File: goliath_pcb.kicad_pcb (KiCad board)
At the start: 2 copper layers, 140 x 90 mm, 95 parts, among them IC1 MCT9001, IC2 MCT9001SD, IC3 MCT9001SD, IC4 MCT9001SD, IC5 MCT9001SD, IC6 MCT9001SD, IC7 MCT9001SD, J1 RJ45_LED, J10 Conn_01x04_Male, J11 Screw_Terminal_01x02, J12 Screw_Terminal_01x02, J13 Screw_Terminal_01x02, J14 Conn_01x02_Male, J15 Conn_01x02_Male, J2 RJ45_LED, J3 RJ45_LED, J4 RJ45_LED, J5 Conn_01x08_Male, J6 Conn_01x08_Male, J7 Conn_01x02_Male, J8 Conn_01x04_Male, J9 Conn_01x04_Male, Q1 STP2N80K5, Q2 STP2N80K5, U1 Pico, U2 LM2592HVT-5.0/NOPB, U3 74HCT244, U4 74HCT244, U5 MCP3008, U6 PCF8574, U7 PCF8574

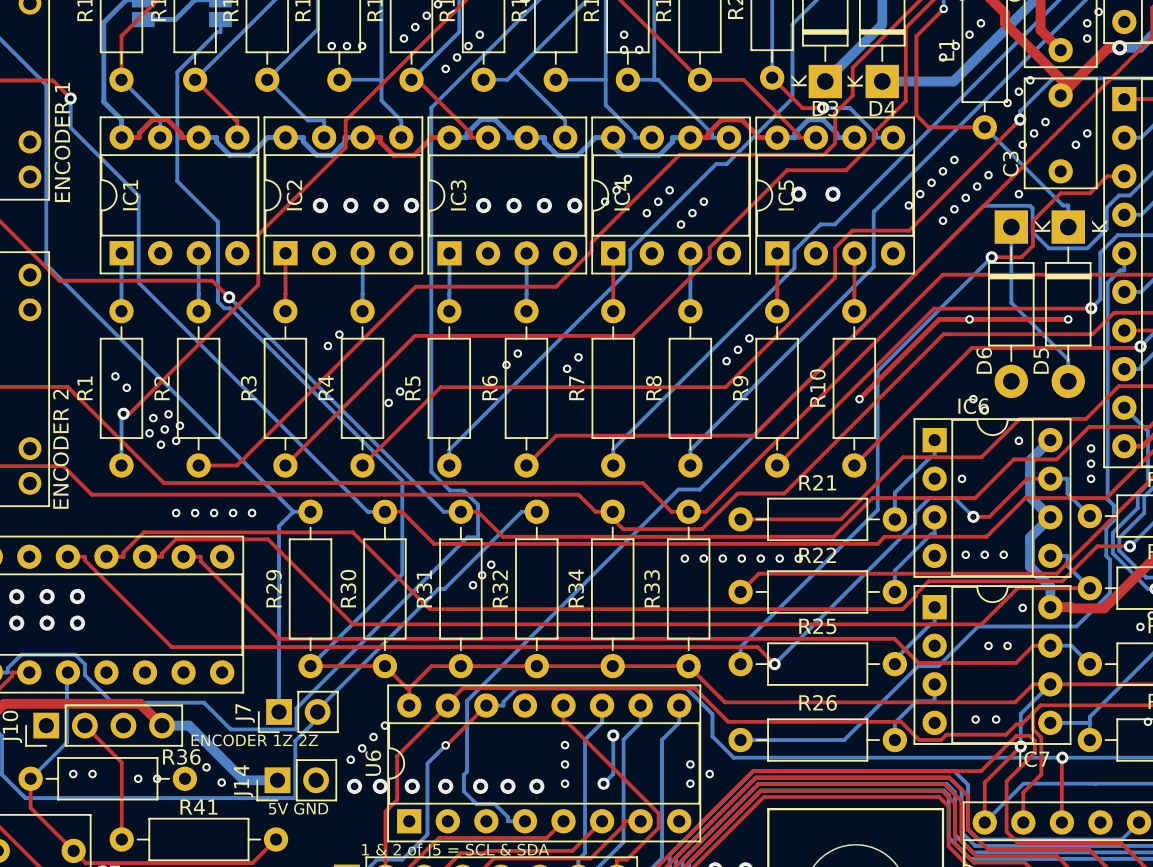
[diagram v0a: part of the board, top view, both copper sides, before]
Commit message: Clean up schematic
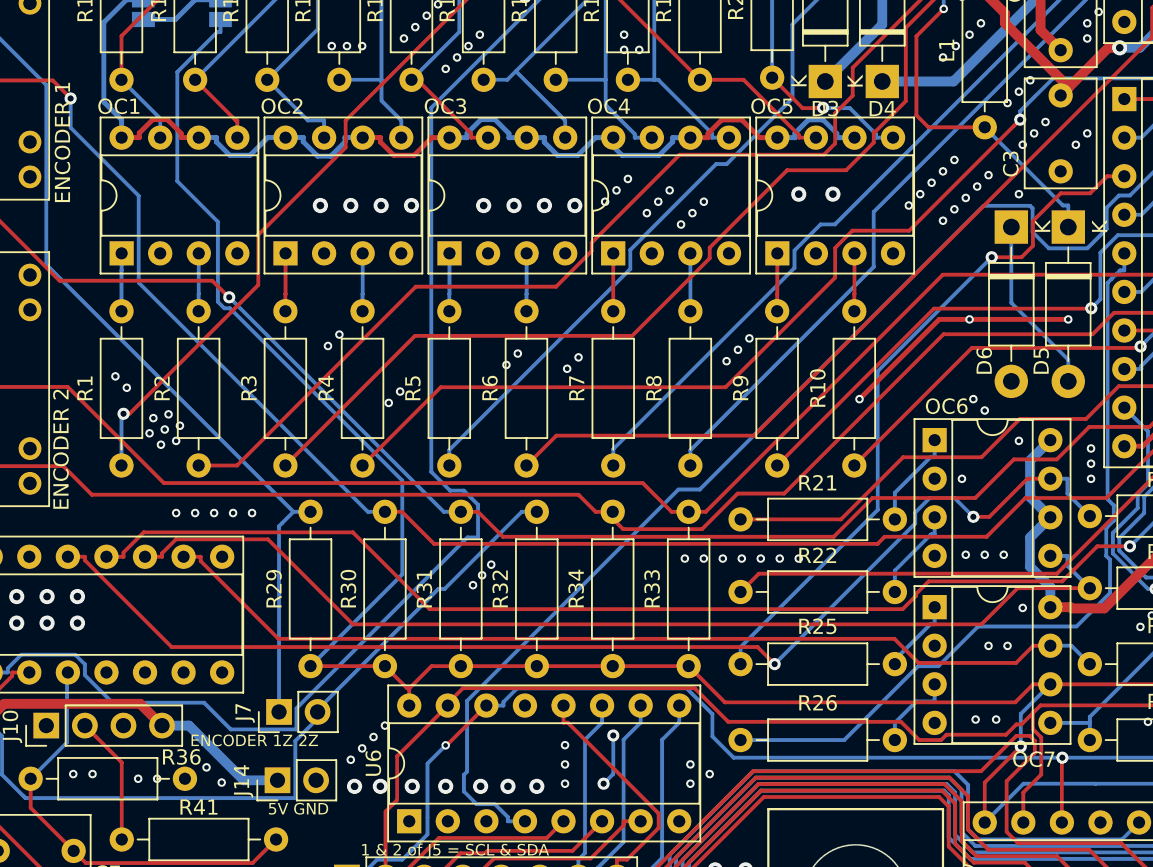
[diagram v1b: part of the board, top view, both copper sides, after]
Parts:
- OC2: renamed from IC2; value MCT9001SD -> MCT9001
- OC3: renamed from IC3; value MCT9001SD -> MCT9001
- OC4: renamed from IC4; value MCT9001SD -> MCT9001
- OC5: renamed from IC5; value MCT9001SD -> MCT9001
- OC6: renamed from IC6; value MCT9001SD -> MCT9001
- OC7: renamed from IC7; value MCT9001SD -> MCT9001
- renumbered IC1 to OC1

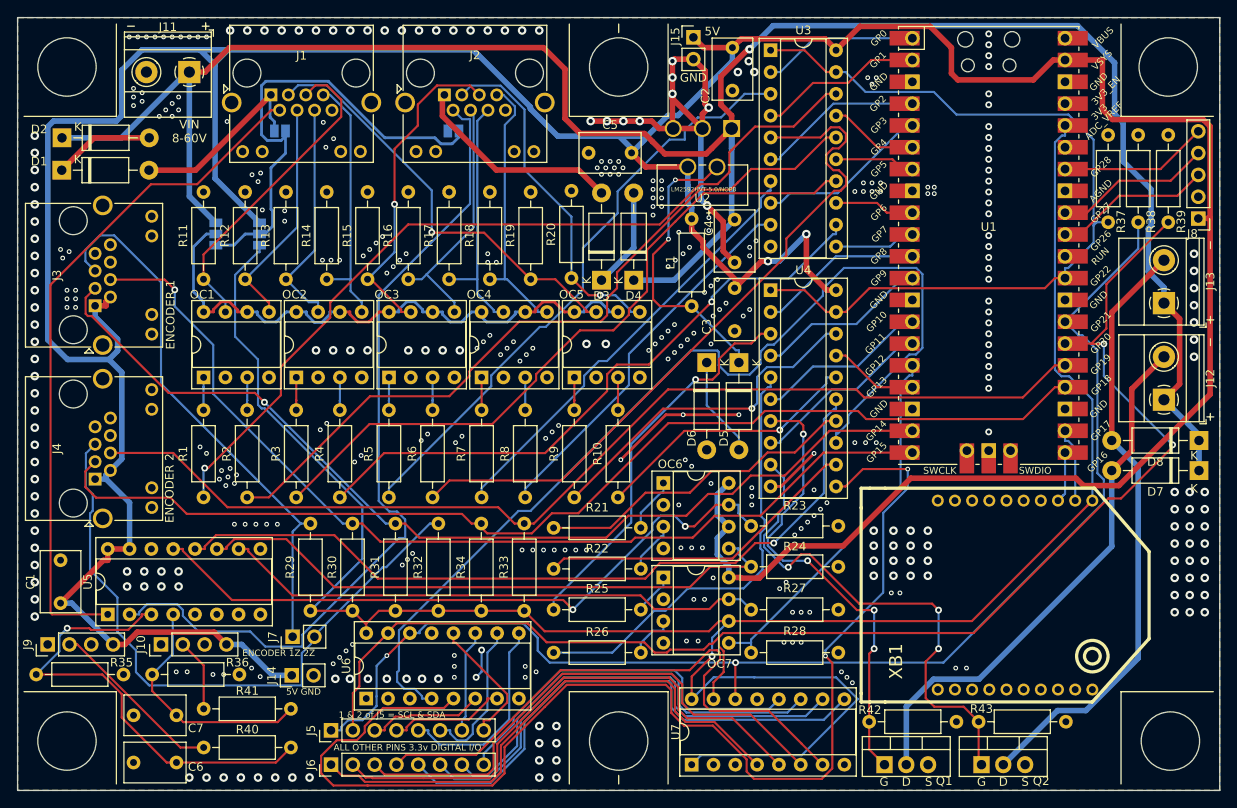
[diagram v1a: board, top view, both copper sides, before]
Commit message: Add proper M4 mounting holes
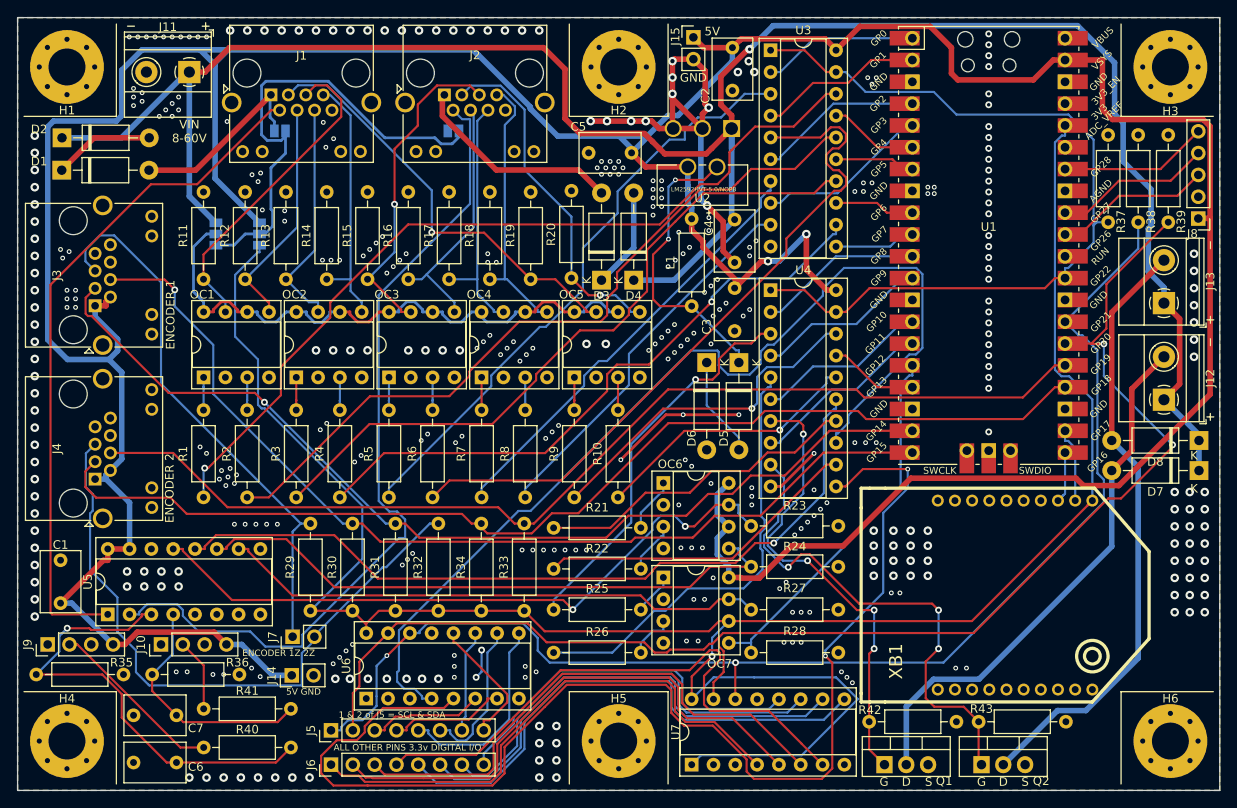
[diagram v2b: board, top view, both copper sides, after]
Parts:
- added H1: MountingHole_Pad, MountingHole:MountingHole_4.3mm_M4_Pad_Via, F.Cu at (41.2, 52.8)
- added H2: MountingHole_Pad, MountingHole:MountingHole_4.3mm_M4_Pad_Via, F.Cu at (105.5, 52.8)
- added H3: MountingHole_Pad, MountingHole:MountingHole_4.3mm_M4_Pad_Via, F.Cu at (169.8, 52.8)
- added H4: MountingHole_Pad, MountingHole:MountingHole_4.3mm_M4_Pad_Via, F.Cu at (41.2, 131.2)
- added H5: MountingHole_Pad, MountingHole:MountingHole_4.3mm_M4_Pad_Via, F.Cu at (105.5, 131.2)
- added H6: MountingHole_Pad, MountingHole:MountingHole_4.3mm_M4_Pad_Via, F.Cu at (169.8, 131.2)
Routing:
- net GND: vias 400 -> 397
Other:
- outline, holes or cut-outs redrawn

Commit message: Fix silkscreen issues
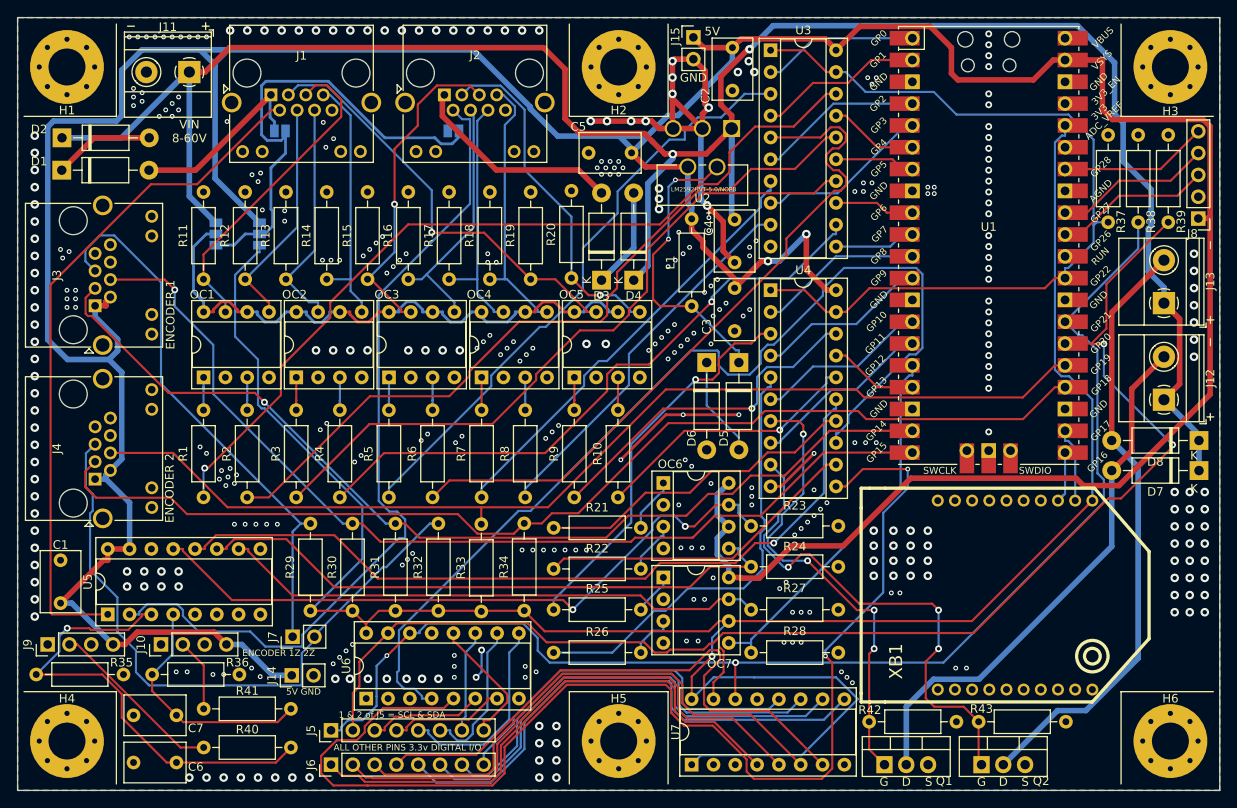
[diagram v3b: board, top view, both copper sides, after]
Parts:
- moved R33 5.00 mm to (89.5, 116.2)
- moved R34 5.00 mm to (94.5, 116.1)
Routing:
- net VIN: track 249.4 -> 251.3 mm, vias 1 -> 2
- net Net-(J4-Pad4): track 123.0 -> 123.9 mm
- net GND: vias 397 -> 391
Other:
- board text added: "Designed by Amelia Deck for ILLINOIS TECH ROBOTICS Robot Interfacing Board (RIB) V1.0-RC1"
- board text removed: "Designed by Amelia Deck for ILLINOIS TECH ROBOTICS Robot interfacing PCB V1.0-RC1"

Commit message: Prepare to swap out diodes
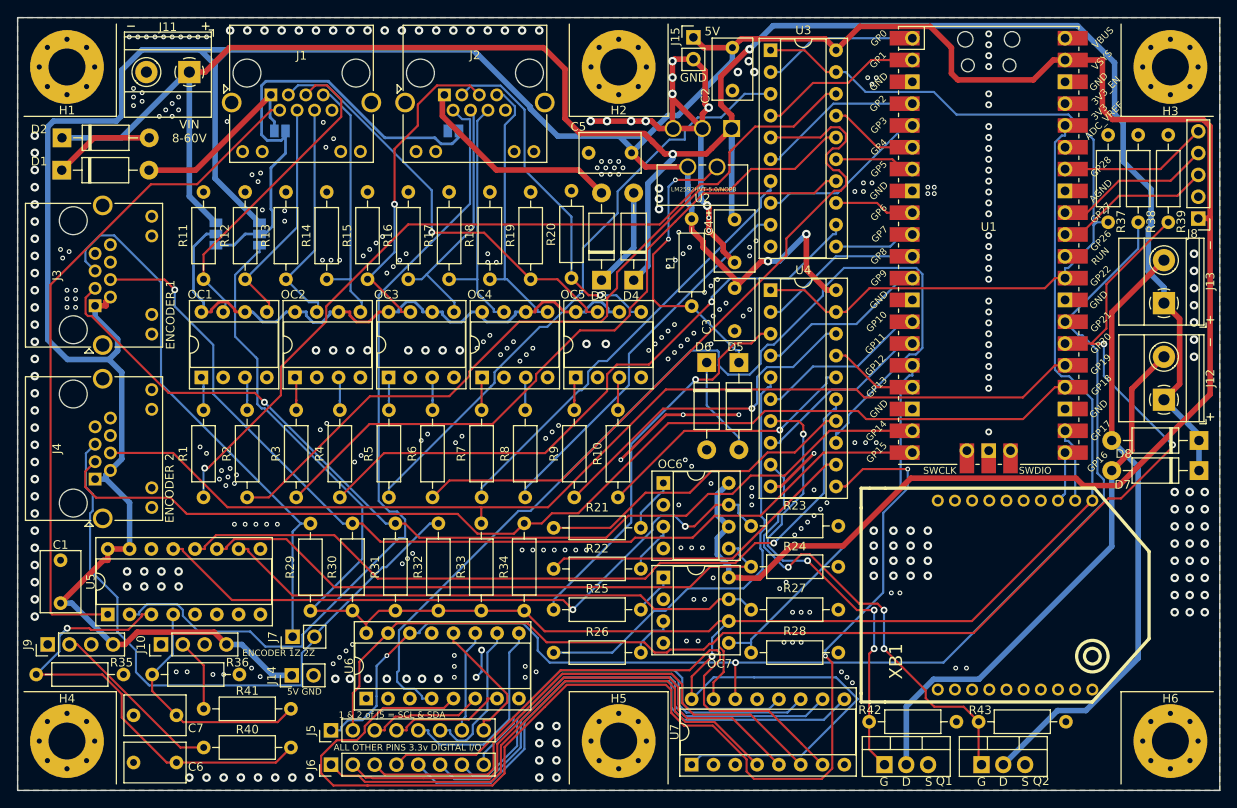
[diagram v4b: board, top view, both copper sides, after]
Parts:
- moved OC1 0.26 mm to (56.9, 88.9)
- moved OC5 0.16 mm to (100.5, 88.9)
- moved OC2 0.16 mm to (67.8, 88.9)
- moved R33 0.10 mm to (89.5, 116.1)
- moved OC4 0.06 mm to (89.6, 88.9)
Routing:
- net Net-(Q2-Pad1): track 59.1 -> 54.2 mm
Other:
- board text added: "GP28 GP27 GP26 GND 5V"

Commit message: Switch to better diodes, use via stitching plugin
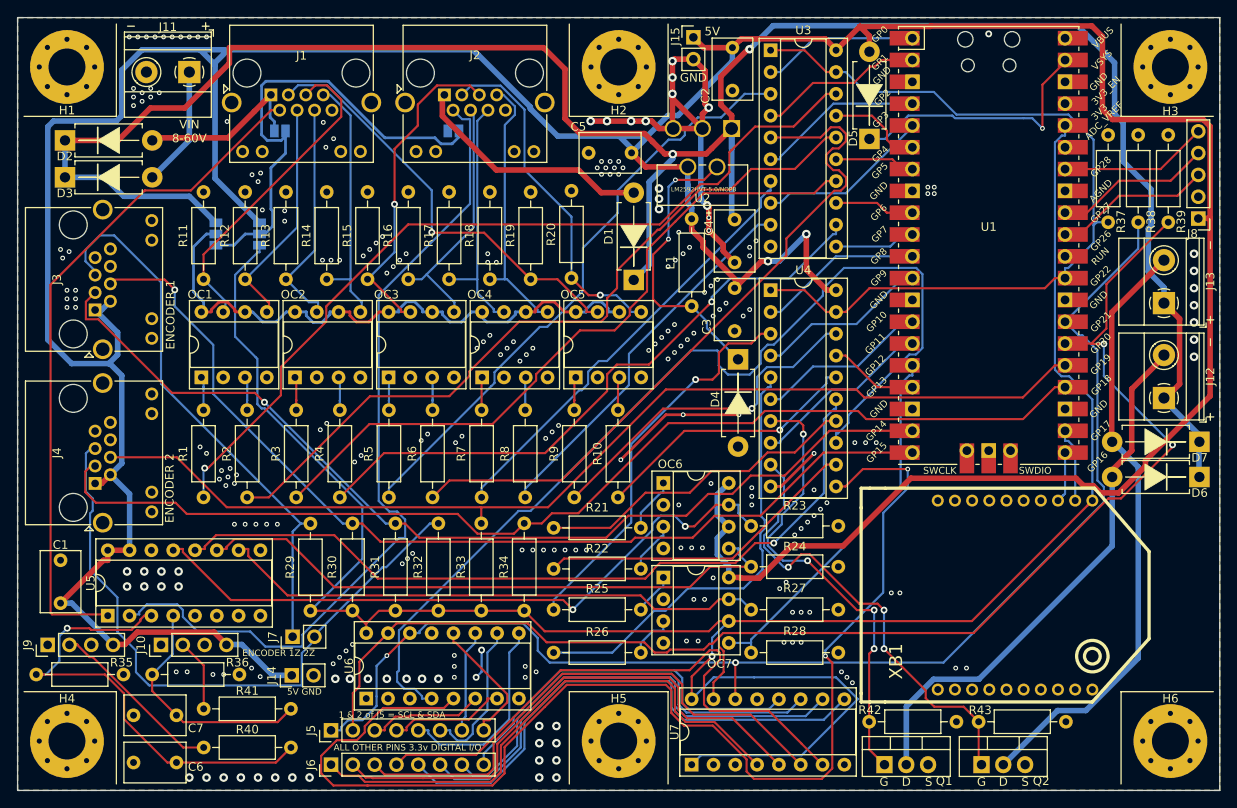
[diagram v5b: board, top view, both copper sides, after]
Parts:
- removed the D5 at (119.5, 87.2)
- removed D8: 1N5819, Diode_THT:D_DO-41_SOD81_P10.16mm_Horizontal
- added D3: SB260, Diode_THT_AKL:D_DO-15_P10.16mm_Horizontal, F.Cu at (41.0, 65.6)
- D1: renamed from D3; value 1N5819 -> SB260; footprint Diode_THT:D_DO-41_SOD81_P10.16mm_Horizontal -> Diode_THT_AKL:D_DO-15_P10.16mm_Horizontal
- D2, D6, D7: value 1N5819 -> SB260; footprint Diode_THT:D_DO-41_SOD81_P10.16mm_Horizontal -> Diode_THT_AKL:D_DO-15_P10.16mm_Horizontal
- D4: value 1N5819 -> SB220; footprint Diode_THT:D_DO-41_SOD81_P10.16mm_Horizontal -> Diode_THT_AKL:D_DO-15_P10.16mm_Horizontal
- D5: renamed from D1; value 1N5819 -> SB220; footprint Diode_THT:D_DO-41_SOD81_P10.16mm_Horizontal -> Diode_THT_AKL:D_DO-15_P10.16mm_Horizontal
- moved D5 94.1 mm to (134.7, 61.1), turned to 90 degrees
- moved D6 58.9 mm to (173.1, 100.5), turned to 180 degrees
- moved D4 15.3 mm to (119.4, 86.8), turned to -90 degrees
- moved D1 3.75 mm to (107.2, 77.5)
- moved D7 3.35 mm to (173.1, 96.4)
- moved J4 0.50 mm to (44.5, 101.2)
- moved J3 0.49 mm to (44.5, 81.0)
- moved D2 0.46 mm to (41.0, 61.3)
- moved J12 0.20 mm to (169.0, 91.3)
- moved U5 0.15 mm to (46.0, 116.7)
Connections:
- D1 pad 1: Net-(D3-Pad1) -> VIN
- D2 pad 2: Net-(D1-Pad1) -> Net-(D2-Pad2)
- D4 pad 1: VIN -> Net-(D4-Pad1)
- D4 pad 2: Net-(D3-Pad1) -> GND
- D5 pad 1: Net-(D1-Pad1) -> Net-(D5-Pad1)
- D5 pad 2: Net-(D1-Pad2) (its old number) -> 5V
- D6 pad 1: Net-(D5-Pad2) -> VIN
- D6 pad 2: GND -> Net-(D6-Pad2)
- J1 pad 1: Net-(D1-Pad2) (its old number) -> Net-(D2-Pad2)
- J11 pad 1: VIN -> Net-(D3-Pad2)
- J12 pad 2: Net-(D7-Pad2) -> Net-(D6-Pad2)
- J13 pad 2: Net-(D8-Pad2) -> Net-(D7-Pad2)
- JP3 pad 1: Net-(D1-Pad2) (its old number) -> Net-(D2-Pad2)
- L1 pad 1: Net-(D5-Pad1) -> Net-(D4-Pad1)
- Q1 pad 2: Net-(D7-Pad2) -> Net-(D6-Pad2)
- Q2 pad 2: Net-(D8-Pad2) -> Net-(D7-Pad2)
- U1 pad 39: 5V -> Net-(D5-Pad1)
- U2 pad 2: Net-(D5-Pad1) -> Net-(D4-Pad1)
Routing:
- net Net-(D8-Pad2): track 71.0 -> 0.00 mm
- net Net-(D6-Pad2): track 0.00 -> 62.3 mm
- net Net-(D4-Pad1): track 0.00 -> 33.7 mm, vias 0 -> 2
- net Net-(D1-Pad2) (its old number): track 22.3 -> 0.00 mm
- net Net-(D2-Pad2): track 0.00 -> 20.3 mm
- net Net-(D3-Pad2): track 0.00 -> 14.0 mm
- net Net-(D1-Pad1): track 11.8 -> 0.00 mm
- net Net-(D5-Pad2): track 11.7 -> 0.00 mm
- net Net-(D3-Pad1): track 11.7 -> 0.00 mm
- net Net-(D7-Pad2): track 63.0 -> 71.0 mm
- net VIN: track 251.3 -> 257.4 mm
- net Net-(D1-Pad2): track 29.3 -> 33.1 mm
- net Net-(D5-Pad1): track 34.3 -> 30.9 mm, vias 2 -> 1
- net 5V: track 468.6 -> 471.2 mm
- net Net-(C6-Pad2): track 53.9 -> 54.6 mm
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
